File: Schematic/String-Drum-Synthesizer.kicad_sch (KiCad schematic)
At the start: 0 parts

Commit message: Power block done
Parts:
- added C1, C3: 0.1uF, symbol Device:C
- added C2, C4: 10uF, symbol Device:C_Polarized
- added R1: 2k, symbol Device:R
- added R2: 3.3k, symbol Device:R
- added U1: LM1117MP-3.3, Package_TO_SOT_SMD:SOT-223-3_TabPin2, symbol Regulator_Linear:LM1117MP-3.3
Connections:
- new net: C3.1, R1.2, R2.1, U1.1 (GND)
- new net +3V3: C4.1, R1.1, U1.2 (VO)
- new net +5V: C1.1, C2.1, U1.3 (VI)
- new net GND: C1.2, C2.2, C3.2, C4.2, R2.2
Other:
- note added: "Power Block"

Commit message: Emotive Knobs in progress
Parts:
- added R3, R4, R5, R6: 16, symbol Device:R
- added U2: OPA1679, symbol Amplifier_Operational:OPA1679
- added U3: CD4051B, symbol Analog_Switch:CD4051B
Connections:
- new net: R3.2, R4.1, R5.2, R6.2, U2.13 (-)
- new net: R4.2, U2.14

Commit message: Emotive Knob subsytem added
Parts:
- removed U3: CD4051B, symbol Analog_Switch:CD4051B
- added Pot0, Pot1, Pot2, Pot3, Pot4, Pot5, Pot6, Pot7: EmotiveKnob, symbol Connector:Conn_01x03_Pin
- added R7, R8: 33, symbol Device:R
- added U3: 74HC4051, symbol 74xx:74HC4051
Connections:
- net +3V3: now also Pot0.1 (Pin_1), Pot1.1 (Pin_1), Pot2.1 (Pin_1), Pot3.1 (Pin_1), Pot4.1 (Pin_1), Pot5.1 (Pin_1), Pot6.1 (Pin_1), Pot7.1 (Pin_1), R7.2, U3.16 (VCC)
- net GND: now also Pot0.3 (Pin_3), Pot1.3 (Pin_3), Pot2.3 (Pin_3), Pot3.3 (Pin_3), Pot4.3 (Pin_3), Pot5.3 (Pin_3), Pot6.3 (Pin_3), Pot7.3 (Pin_3), R8.1, U3.6 (~{E}), U3.7 (VEE)
- new net: Pot6.2 (Pin_2), U3.2 (A6)
- new net: Pot0.2 (Pin_2), U3.13 (A0)
- new net: Pot7.2 (Pin_2), U3.4 (A7)
- new net: R7.1, R8.2, U3.8 (GND)
- new net: Pot4.2 (Pin_2), U3.1 (A4)
- new net: Pot3.2 (Pin_2), U3.12 (A3)
- new net: Pot1.2 (Pin_2), U3.14 (A1)
- new net: Pot2.2 (Pin_2), U3.15 (A2)
- new net: Pot5.2 (Pin_2), U3.5 (A5)
- new net EmotiveKnobKey0: U3.11 (S0)
- new net EmotiveKnobKey1: U3.10 (S1)
- new net EmotiveKnobKey2: U3.9 (S2)
- new net EmotiveKnobValue: U3.3 (A)
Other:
- note added: "Emotive Knobs"
- moved on the sheet: R3, R4, R5, R6, U2A, U2B, U2C, U2D

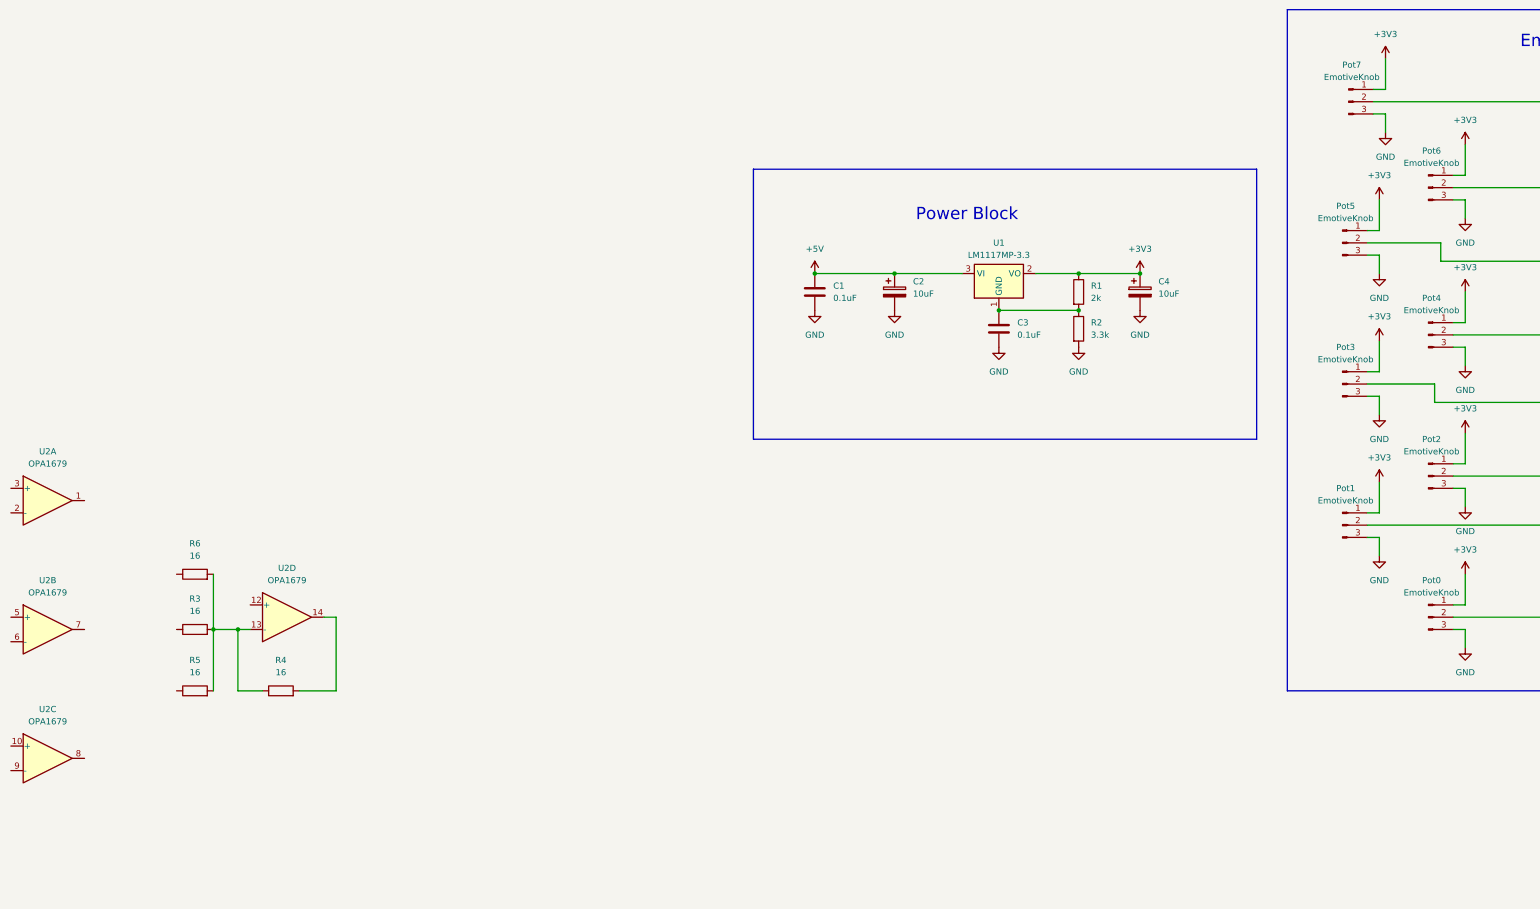
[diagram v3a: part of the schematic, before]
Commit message: Amplifier subsystem added
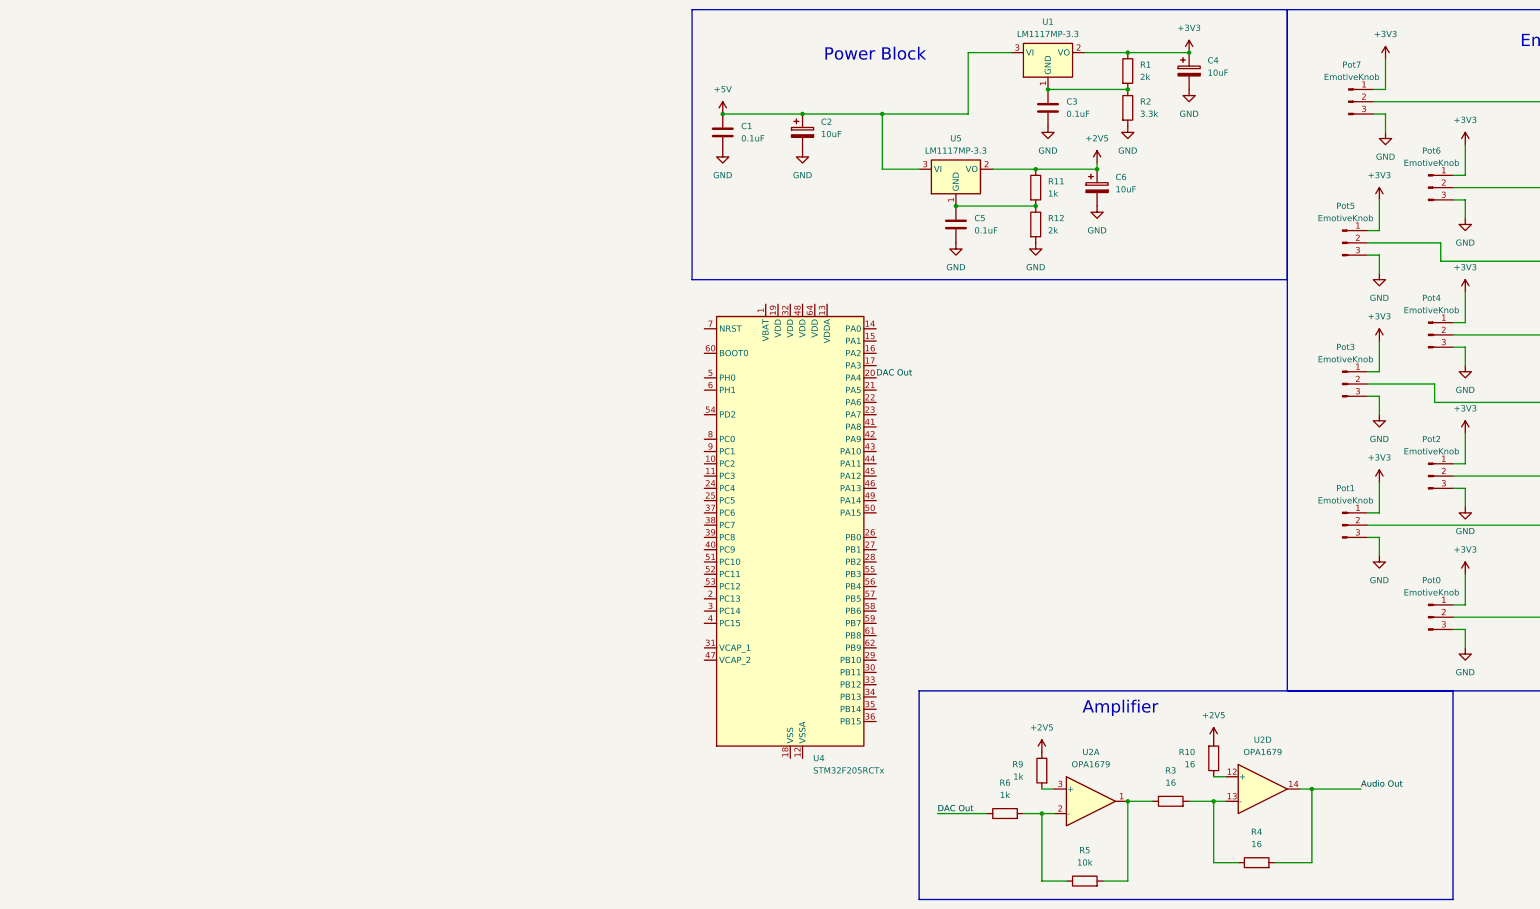
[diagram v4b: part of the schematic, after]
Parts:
- removed unit 3 of U2
- removed unit 2 of U2
- added C5: 0.1uF, symbol Device:C
- added C6: 10uF, symbol Device:C_Polarized
- added R10: 16, symbol Device:R
- added R11, R9: 1k, symbol Device:R
- added R12: 2k, symbol Device:R
- added U4: STM32F205RCTx, Package_QFP:LQFP-64_10x10mm_P0.5mm, symbol MCU_ST_STM32F2:STM32F205RCTx
- added U5: LM1117MP-3.3, Package_TO_SOT_SMD:SOT-223-3_TabPin2, symbol Regulator_Linear:LM1117MP-3.3
- R5: value 16 -> 10k
- R6: value 16 -> 1k
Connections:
- net +5V: now also U5.3 (VI)
- net GND: now also C5.2, C6.2, R12.2
- net at R3.2, R4.1, U2.13 (-): no longer R5.2, R6.2
- net Audio Out: now reaches R4.2, U2.14
- net DAC Out: now reaches R6.1
- net DAC Out: now also U4.20 (PA4)
- net at U2.12 (+): now also R10.1
- net at U2.1: now also R3.1, R5.2
- net at U2.2 (-): now also R5.1, R6.2
- net at U2.3 (+): now also R9.2
- new net: C5.1, R11.2, R12.1, U5.1 (GND)
- new net: U4.18 (VSS), U4.63 (VSS)
- new net +2V5: C6.1, R10.2, R11.1, R9.1, U5.2 (VO)
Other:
- note added: "Amplifier"
- moved on the sheet: C1, C2, C3, C4, R1, R2, R3, R4, U1, U2A, U2D
